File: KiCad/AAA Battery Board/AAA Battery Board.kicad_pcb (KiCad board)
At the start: 2 copper layers, 73.7 x 50.9 mm, 6 parts, among them J1 To Mobo

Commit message: update files
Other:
- board text added: "JLCJLCJLCJLC"
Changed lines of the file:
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@@
+    (effects (font (size 1 1) (thickness 0.15)) (justify left bottom))
+  )
+  (gr_text "JLCJLCJLCJLC" (at 135.73 75.86) (layer "F.SilkS")
     (effects (font (size 1 1) (thickness 0.15)) (justify left bottom))
   )

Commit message: Add zip tie holes
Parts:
- 3 x AAA (~4.5V): renamed from 3 x AAA (4.5V)
- D1: value 1N5817 -> 1N4148; footprint Diode_THT:D_DO-41_SOD81_P7.62mm_Horizontal -> Diode_THT:D_DO-35_SOD27_P7.62mm_Horizontal
- moved Open Hardware Logo 58.1 mm to (111.0, 83.0)
- moved KiCad Logo 37.9 mm to (122.0, 72.0)
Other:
- outline, holes or cut-outs redrawn
- board text added: "3 x AAA remote battery board for retro PCs. Please double check polarity before installing. Not responsible for improper installation. Please read all documentation. When mounting with dbl sided tape or Velcro, please also use a layer of Kapton tape for extra insulation. Designed, assembled, and tested in the USA with global parts."
- board text removed: "3 x AAA remote battery board for retro PCs. For motherboards with 4-pin 2.54mm external battery headers. 1N5817 diode prevents charging and has low voltage drop. Powers RTC/NVRAM. (Also called CMOS/BIOS/Mobo battery) Most motherboards require between 3V and 6V. Please double check polarity before installing. Not responsible for improper installation. Please read all documentation. When mounting w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"

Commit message: fix typos
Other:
- board text added: "F1: 5mm x 20mm 100mA"
- board text added: "WayWayWay"
- board text removed: "F1: 5mm x 20mm 100ma"
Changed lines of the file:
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@@
     (effects (font (size 1 1) (thickness 0.15)) (justify left bottom mirror))
   )
-  (gr_text "F1: 5mm x 20mm 100ma" (at 118 58.293) (layer "F.SilkS")
+  (gr_text "F1: 5mm x 20mm 100mA" (at 118 58.293) (layer "F.SilkS")
     (effects (font (size 1.2 1.2) (thickness 0.24) bold) (justify left bottom))
   )
@@
     (effects (font (size 1 1) (thickness 0.15)) (justify left bottom))
   )
+  (gr_text "WayWayWay" (at 137 79.5) (layer "F.SilkS")
+    (effects (font (size 1 1) (thickness 0.15)) (justify left bottom))
+  )

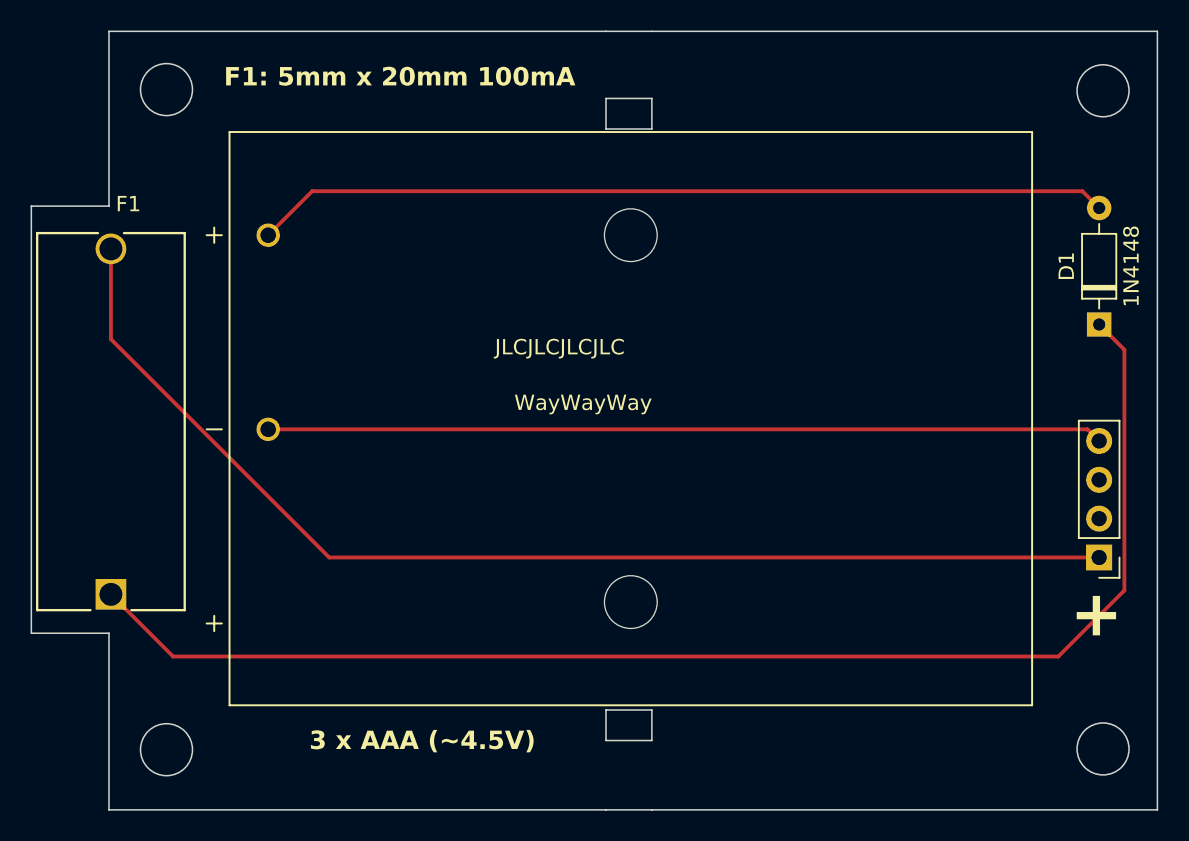
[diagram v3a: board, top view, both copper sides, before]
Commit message: Update footprints.
Update fuse holder footprint to work with both 15mm and 23mm leg spacing versions.
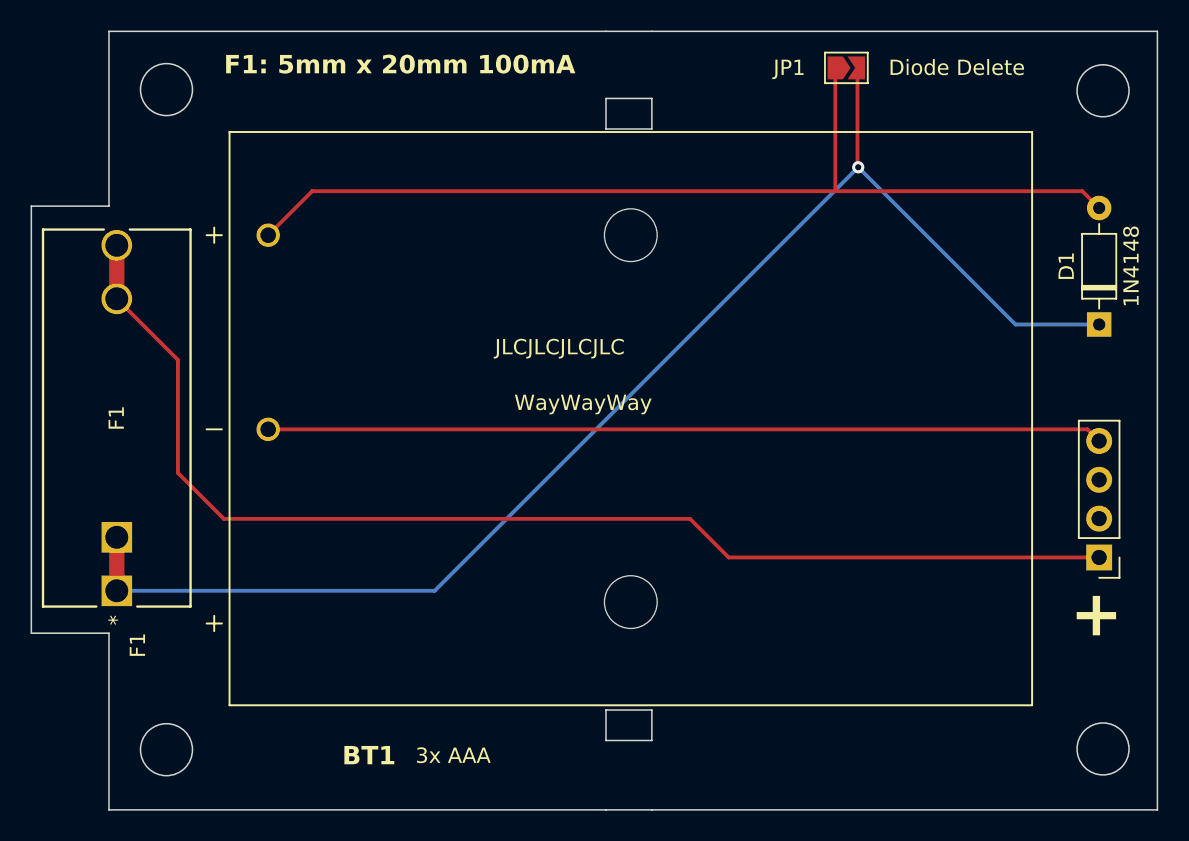
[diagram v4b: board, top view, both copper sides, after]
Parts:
- added JP1: Diode Delete, Jumper:SolderJumper-2_P1.3mm_Open_TrianglePad1.0x1.5mm, F.Cu at (158.7, 57.0)
- BT1: renamed from 3 x AAA (~4.5V); value 2479 -> 3x AAA
- F1: value 0PTF0078P -> 100mA; footprint footprints:FUSE_0PTF0078P_LTF -> PCRestoLib:UniversalGreenFuseHolder
- moved F1 0.45 mm to (111.0, 91.2)
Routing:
- net Net-(D1-A): track 56.0 -> 64.1 mm
- net Net-(J1-Pin_1): track 76.5 -> 74.8 mm
- net Net-(D1-K): track 87.8 -> 86.5 mm, vias 0 -> 1
